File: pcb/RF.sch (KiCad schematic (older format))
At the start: 50 parts, among them P401 CONN_01X02, P402 CONN_01X02, U401 MAX2750, U402 MGA-635P8, U403 HHM1520, U404 MGA-635P8, U405 LT5560, U406 PD2328J, U407 WA04P

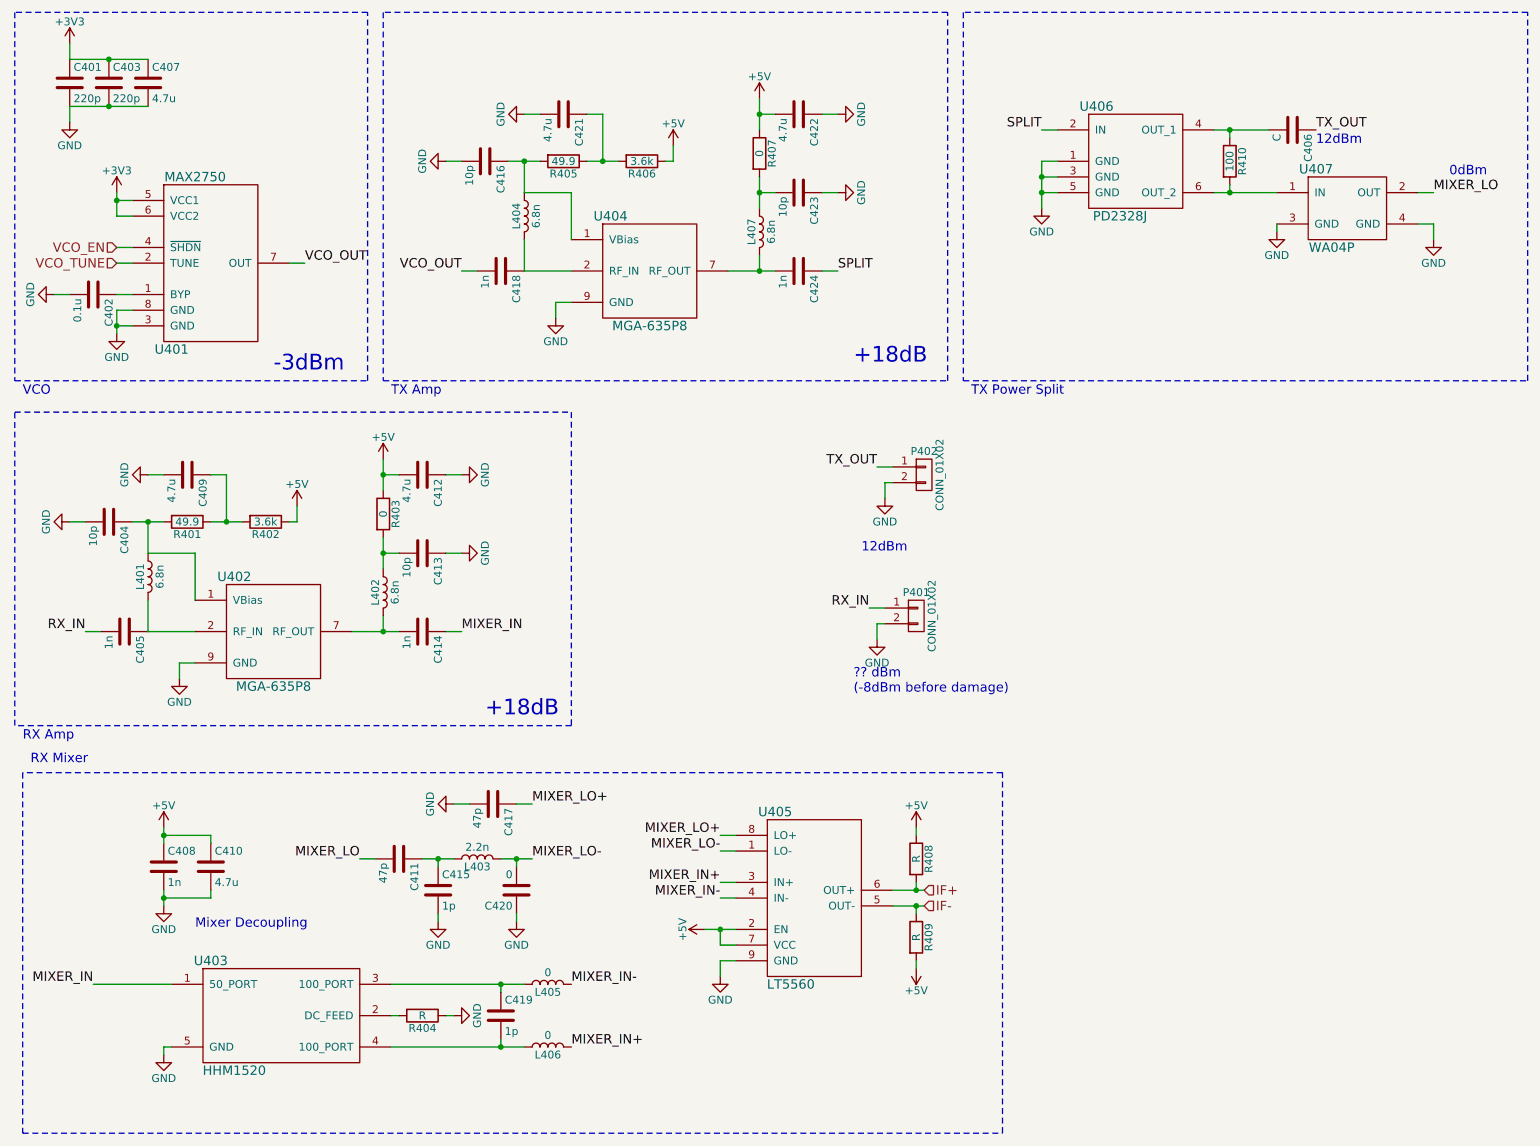
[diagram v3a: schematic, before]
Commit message: First firmware to begin board bringup
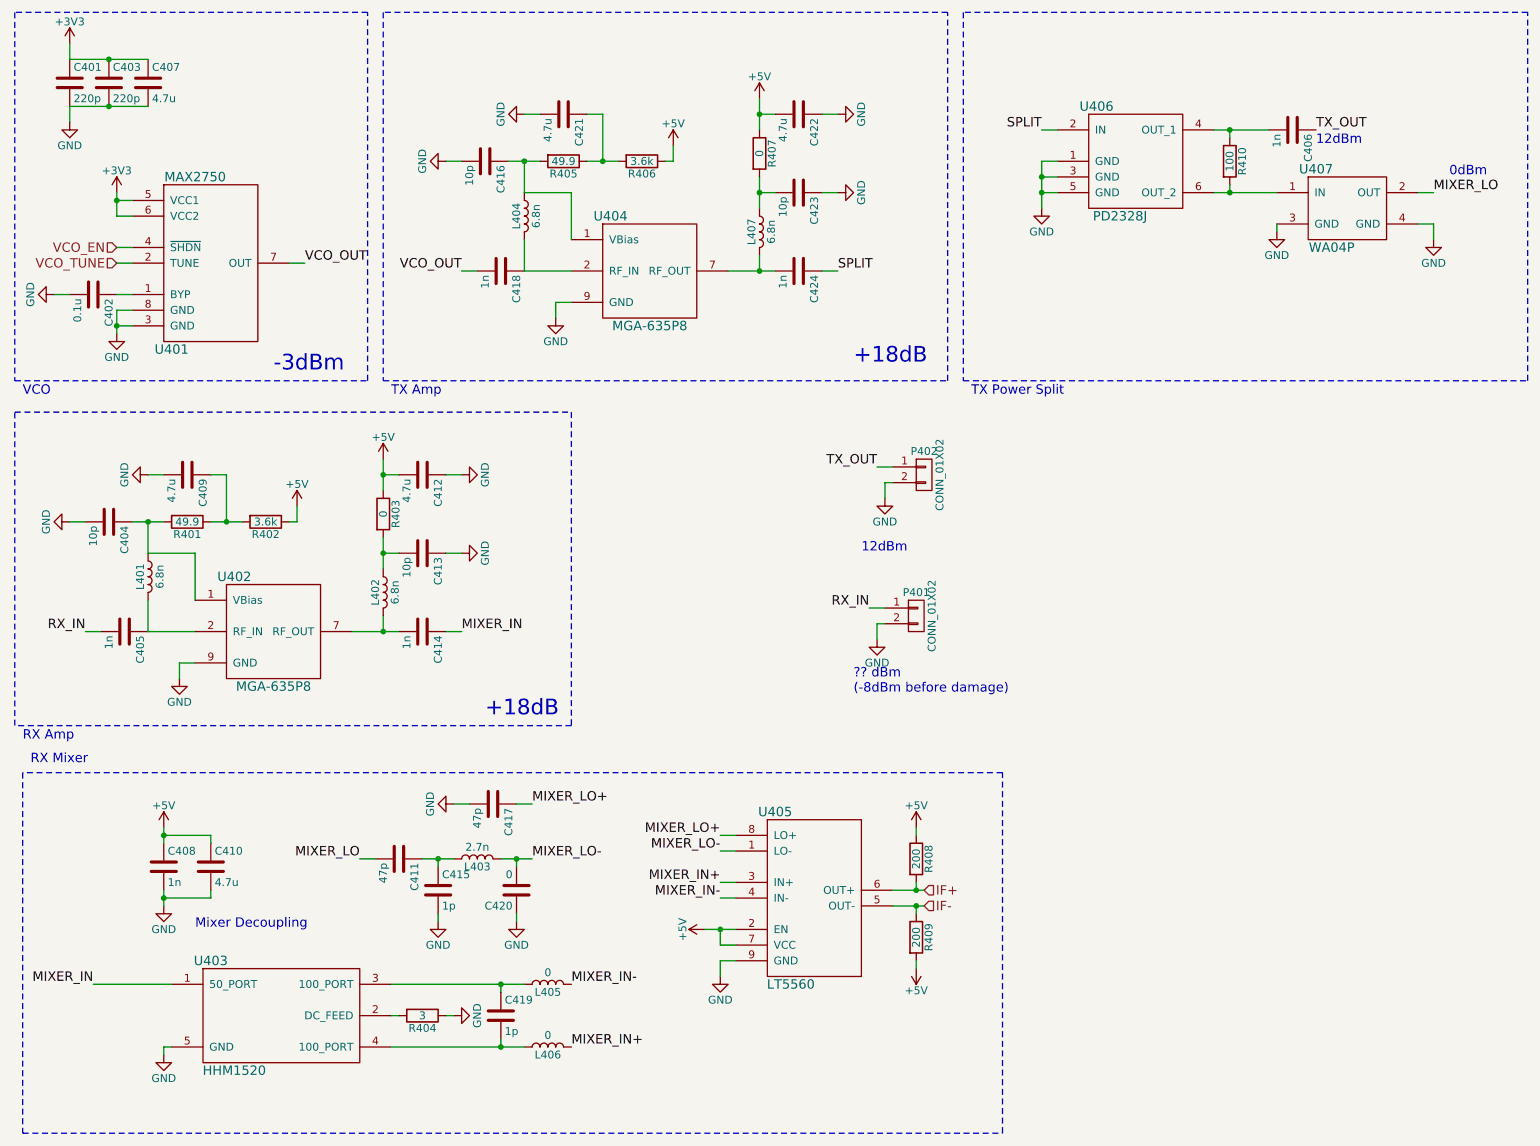
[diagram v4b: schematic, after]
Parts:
- C406: value C -> 1n
- L403: value 2.2n -> 2.7n
- R404: value R -> 3
- R408, R409: value R -> 200
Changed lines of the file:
@@
 $EndComp
 $Comp
-L GND #PWR411
+L GND #PWR043
 U 1 1 58AA10B9
 P 1600 4800
-F 0 "#PWR411" H 1600 4550 50  0001 C CNN
+F 0 "#PWR043" H 1600 4550 50  0001 C CNN
 F 1 "GND" H 1600 4650 50  0000 C CNN
 F 2 "" H 1600 4800 50  0000 C CNN
@@
 $EndComp
 $Comp
-L GND #PWR404
+L GND #PWR044
 U 1 1 58AA10EF
 P 900 3800
-F 0 "#PWR404" H 900 3550 50  0001 C CNN
+F 0 "#PWR044" H 900 3550 50  0001 C CNN
 F 1 "GND" H 900 3650 50  0000 C CNN
 F 2 "" H 900 3800 50  0000 C CNN
@@
 $EndComp
 $Comp
-L GND #PWR407
+L GND #PWR045
 U 1 1 58AA1125
 P 1400 3500
-F 0 "#PWR407" H 1400 3250 50  0001 C CNN
+F 0 "#PWR045" H 1400 3250 50  0001 C CNN
 F 1 "GND" H 1400 3350 50  0000 C CNN
 F 2 "" H 1400 3500 50  0000 C CNN
@@
 $EndComp
 $Comp
-L GND #PWR419
+L GND #PWR046
 U 1 1 58AA115B
 P 3400 4000
-F 0 "#PWR419" H 3400 3750 50  0001 C CNN
+F 0 "#PWR046" H 3400 3750 50  0001 C CNN
 F 1 "GND" H 3400 3850 50  0000 C CNN
 F 2 "" H 3400 4000 50  0000 C CNN
@@
 $EndComp
 $Comp
-L GND #PWR418
+L GND #PWR047
 U 1 1 58AA1191
 P 3400 3500
-F 0 "#PWR418" H 3400 3250 50  0001 C CNN
+F 0 "#PWR047" H 3400 3250 50  0001 C CNN
 F 1 "GND" H 3400 3350 50  0000 C CNN
 F 2 "" H 3400 3500 50  0000 C CNN
@@
 $EndComp
 $Comp
-L +5V #PWR413
+L +5V #PWR048
 U 1 1 58AA11C7
 P 2900 3400
-F 0 "#PWR413" H 2900 3250 50  0001 C CNN
+F 0 "#PWR048" H 2900 3250 50  0001 C CNN
 F 1 "+5V" H 2900 3540 50  0000 C CNN
 F 2 "" H 2900 3400 50  0000 C CNN
@@
 $EndComp
 $Comp
-L +5V #PWR412
+L +5V #PWR049
 U 1 1 58AA11FD
 P 2350 3700
-F 0 "#PWR412" H 2350 3550 50  0001 C CNN
+F 0 "#PWR049" H 2350 3550 50  0001 C CNN
 F 1 "+5V" H 2350 3840 50  0000 C CNN
 F 2 "" H 2350 3700 50  0000 C CNN
@@
 P 3150 6950
 F 0 "R404" V 3230 6950 50  0000 C CNN
-F 1 "R" V 3150 6950 50  0000 C CNN
+F 1 "3" V 3150 6950 50  0000 C CNN
 F 2 "Resistors_SMD:R_0402" V 3080 6950 50  0001 C CNN
 F 3 "" H 3150 6950 50  0000 C CNN
@@
 $EndComp
 $Comp
-L GND #PWR417
+L GND #PWR050
 U 1 1 58AA2399
 P 3350 6950
-F 0 "#PWR417" H 3350 6700 50  0001 C CNN
+F 0 "#PWR050" H 3350 6700 50  0001 C CNN
 F 1 "GND" H 3350 6800 50  0000 C CNN
 F 2 "" H 3350 6950 50  0000 C CNN
@@
 P 3500 5950
 F 0 "L403" V 3450 5950 50  0000 C CNN
-F 1 "2.2n" V 3575 5950 50  0000 C CNN
+F 1 "2.7n" V 3575 5950 50  0000 C CNN
 F 2 "Capacitors_SMD:C_0402" H 3500 5950 50  0001 C CNN
 F 3 "" H 3500 5950 50  0000 C CNN
@@
 $EndComp
 $Comp
-L GND #PWR420
+L GND #PWR051
 U 1 1 58AA2A6C
 P 3750 6350
-F 0 "#PWR420" H 3750 6100 50  0001 C CNN
+F 0 "#PWR051" H 3750 6100 50  0001 C CNN
 F 1 "GND" H 3750 6200 50  0000 C CNN
 F 2 "" H 3750 6350 50  0000 C CNN
@@
 $EndComp
 $Comp
-L GND #PWR414
+L GND #PWR052
 U 1 1 58AA2AB8
 P 3250 6350
-F 0 "#PWR414" H 3250 6100 50  0001 C CNN
+F 0 "#PWR052" H 3250 6100 50  0001 C CNN
 F 1 "GND" H 3250 6200 50  0000 C CNN
 F 2 "" H 3250 6350 50  0000 C CNN
@@
 $EndComp
 $Comp
-L GND #PWR410
+L GND #PWR053
 U 1 1 58AA2B04
 P 1500 7200
-F 0 "#PWR410" H 1500 6950 50  0001 C CNN
+F 0 "#PWR053" H 1500 6950 50  0001 C CNN
 F 1 "GND" H 1500 7050 50  0000 C CNN
 F 2 "" H 1500 7200 50  0000 C CNN
@@
 $EndComp
 $Comp
-L GND #PWR416
+L GND #PWR054
 U 1 1 58AA32CA
 P 3350 5600
-F 0 "#PWR416" H 3350 5350 50  0001 C CNN
+F 0 "#PWR054" H 3350 5350 50  0001 C CNN
 F 1 "GND" H 3350 5450 50  0000 C CNN
 F 2 "" H 3350 5600 50  0000 C CNN
@@
 MIXER_IN+
 $Comp
-L GND #PWR425
+L GND #PWR055
 U 1 1 58AA3ACB
 P 5050 6700
-F 0 "#PWR425" H 5050 6450 50  0001 C CNN
+F 0 "#PWR055" H 5050 6450 50  0001 C CNN
 F 1 "GND" H 5050 6550 50  0000 C CNN
 F 2 "" H 5050 6700 50  0000 C CNN
@@
 $EndComp
 $Comp
-L GND #PWR409
+L GND #PWR056
 U 1 1 58AA3E57
 P 1500 6250
-F 0 "#PWR409" H 1500 6000 50  0001 C CNN
+F 0 "#PWR056" H 1500 6000 50  0001 C CNN
 F 1 "GND" H 1500 6100 50  0000 C CNN
 F 2 "" H 1500 6250 50  0000 C CNN
@@
 $EndComp
 $Comp
-L +5V #PWR408
+L +5V #PWR057
 U 1 1 58AA4282
 P 1500 5750
-F 0 "#PWR408" H 1500 5600 50  0001 C CNN
+F 0 "#PWR057" H 1500 5600 50  0001 C CNN
 F 1 "+5V" H 1500 5890 50  0000 C CNN
 F 2 "" H 1500 5750 50  0000 C CNN
@@
 $EndComp
 $Comp
-L +5V #PWR424
+L +5V #PWR058
 U 1 1 58AA42F1
 P 4950 6400
-F 0 "#PWR424" H 4950 6250 50  0001 C CNN
+F 0 "#PWR058" H 4950 6250 50  0001 C CNN
 F 1 "+5V" H 4950 6540 50  0000 C CNN
 F 2 "" H 4950 6400 50  0000 C CNN
@@
 P 6300 6450
 F 0 "R409" V 6380 6450 50  0000 C CNN
-F 1 "R" V 6300 6450 50  0000 C CNN
+F 1 "200" V 6300 6450 50  0000 C CNN
 F 2 "Resistors_SMD:R_0402" V 6230 6450 50  0001 C CNN
 F 3 "" H 6300 6450 50  0000 C CNN
@@
 P 6300 5950
 F 0 "R408" V 6380 5950 50  0000 C CNN
-F 1 "R" V 6300 5950 50  0000 C CNN
+F 1 "200" V 6300 5950 50  0000 C CNN
 F 2 "Resistors_SMD:R_0402" V 6230 5950 50  0001 C CNN
 F 3 "" H 6300 5950 50  0000 C CNN
@@
 $EndComp
 $Comp
-L +5V #PWR432
+L +5V #PWR059
 U 1 1 58AA4D6B
 P 6300 6650
-F 0 "#PWR432" H 6300 6500 50  0001 C CNN
+F 0 "#PWR059" H 6300 6500 50  0001 C CNN
 F 1 "+5V" H 6300 6790 50  0000 C CNN
 F 2 "" H 6300 6650 50  0000 C CNN
@@
 $EndComp
 $Comp
-L +5V #PWR431
+L +5V #PWR060
 U 1 1 58AA4DBF
 P 6300 5750
-F 0 "#PWR431" H 6300 5600 50  0001 C CNN
+F 0 "#PWR060" H 6300 5600 50  0001 C CNN
 F 1 "+5V" H 6300 5890 50  0000 C CNN
 F 2 "" H 6300 5750 50  0000 C CNN
@@
 $EndComp
 $Comp
-L GND #PWR422
+L GND #PWR061
 U 1 1 58AA62C7
 P 4000 2500
-F 0 "#PWR422" H 4000 2250 50  0001 C CNN
+F 0 "#PWR061" H 4000 2250 50  0001 C CNN
 F 1 "GND" H 4000 2350 50  0000 C CNN
 F 2 "" H 4000 2500 50  0000 C CNN
@@
 $EndComp
 $Comp
-L GND #PWR415
+L GND #PWR062
 U 1 1 58AA62CD
 P 3300 1500
-F 0 "#PWR415" H 3300 1250 50  0001 C CNN
+F 0 "#PWR062" H 3300 1250 50  0001 C CNN
 F 1 "GND" H 3300 1350 50  0000 C CNN
 F 2 "" H 3300 1500 50  0000 C CNN
@@
 $EndComp
 $Comp
-L GND #PWR421
+L GND #PWR063
 U 1 1 58AA62D3
 P 3800 1200
-F 0 "#PWR421" H 3800 950 50  0001 C CNN
+F 0 "#PWR063" H 3800 950 50  0001 C CNN
 F 1 "GND" H 3800 1050 50  0000 C CNN
 F 2 "" H 3800 1200 50  0000 C CNN
@@
 $EndComp
 $Comp
-L GND #PWR428
+L GND #PWR064
 U 1 1 58AA62D9
 P 5800 1700
-F 0 "#PWR428" H 5800 1450 50  0001 C CNN
+F 0 "#PWR064" H 5800 1450 50  0001 C CNN
 F 1 "GND" H 5800 1550 50  0000 C CNN
 F 2 "" H 5800 1700 50  0000 C CNN
@@
 $EndComp
 $Comp
-L GND #PWR427
+L GND #PWR065
 U 1 1 58AA62DF
 P 5800 1200
-F 0 "#PWR427" H 5800 950 50  0001 C CNN
+F 0 "#PWR065" H 5800 950 50  0001 C CNN
 F 1 "GND" H 5800 1050 50  0000 C CNN
 F 2 "" H 5800 1200 50  0000 C CNN
@@
 $EndComp
 $Comp
-L +5V #PWR426
+L +5V #PWR066
 U 1 1 58AA62E5
 P 5300 1100
-F 0 "#PWR426" H 5300 950 50  0001 C CNN
+F 0 "#PWR066" H 5300 950 50  0001 C CNN
 F 1 "+5V" H 5300 1240 50  0000 C CNN
 F 2 "" H 5300 1100 50  0000 C CNN
@@
 $EndComp
 $Comp
-L +5V #PWR423
+L +5V #PWR067
 U 1 1 58AA62EB
 P 4750 1400
-F 0 "#PWR423" H 4750 1250 50  0001 C CNN
+F 0 "#PWR067" H 4750 1250 50  0001 C CNN
 F 1 "+5V" H 4750 1540 50  0000 C CNN
 F 2 "" H 4750 1400 50  0000 C CNN
@@
 $EndComp
 $Comp
-L +3V3 #PWR402
+L +3V3 #PWR068
 U 1 1 58AA6803
 P 900 750
-F 0 "#PWR402" H 900 600 50  0001 C CNN
+F 0 "#PWR068" H 900 600 50  0001 C CNN
 F 1 "+3V3" H 900 890 50  0000 C CNN
 F 2 "" H 900 750 50  0000 C CNN
@@
 $EndComp
 $Comp
-L +3V3 #PWR405
+L +3V3 #PWR069
 U 1 1 58AA6877
 P 1200 1700
-F 0 "#PWR405" H 1200 1550 50  0001 C CNN
+F 0 "#PWR069" H 1200 1550 50  0001 C CNN
 F 1 "+3V3" H 1200 1840 50  0000 C CNN
 F 2 "" H 1200 1700 50  0000 C CNN
@@
 $EndComp
 $Comp
-L GND #PWR403
+L GND #PWR070
 U 1 1 58AA68EB
 P 900 1250
-F 0 "#PWR403" H 900 1000 50  0001 C CNN
+F 0 "#PWR070" H 900 1000 50  0001 C CNN
 F 1 "GND" H 900 1100 50  0000 C CNN
 F 2 "" H 900 1250 50  0000 C CNN
@@
 $EndComp
 $Comp
-L GND #PWR406
+L GND #PWR071
 U 1 1 58AA695F
 P 1200 2600
-F 0 "#PWR406" H 1200 2350 50  0001 C CNN
+F 0 "#PWR071" H 1200 2350 50  0001 C CNN
 F 1 "GND" H 1200 2450 50  0000 C CNN
 F 2 "" H 1200 2600 50  0000 C CNN
@@
 $EndComp
 $Comp
-L GND #PWR401
+L GND #PWR072
 U 1 1 58AA69D3
 P 800 2350
-F 0 "#PWR401" H 800 2100 50  0001 C CNN
+F 0 "#PWR072" H 800 2100 50  0001 C CNN
 F 1 "GND" H 800 2200 50  0000 C CNN
 F 2 "" H 800 2350 50  0000 C CNN
@@
 VCO_OUT
 $Comp
-L GND #PWR433
+L GND #PWR073
 U 1 1 58AA8C7D
 P 7100 1800
-F 0 "#PWR433" H 7100 1550 50  0001 C CNN
+F 0 "#PWR073" H 7100 1550 50  0001 C CNN
 F 1 "GND" H 7100 1650 50  0000 C CNN
 F 2 "" H 7100 1800 50  0000 C CNN
@@
 $EndComp
 $Comp
-L GND #PWR434
+L GND #PWR074
 U 1 1 58AA97AD
 P 8600 1950
-F 0 "#PWR434" H 8600 1700 50  0001 C CNN
+F 0 "#PWR074" H 8600 1700 50  0001 C CNN
 F 1 "GND" H 8600 1800 50  0000 C CNN
 F 2 "" H 8600 1950 50  0000 C CNN
@@
 $EndComp
 $Comp
-L GND #PWR435
+L GND #PWR075
 U 1 1 58AA9851
 P 9600 2000
-F 0 "#PWR435" H 9600 1750 50  0001 C CNN
+F 0 "#PWR075" H 9600 1750 50  0001 C CNN
 F 1 "GND" H 9600 1850 50  0000 C CNN
 F 2 "" H 9600 2000 50  0000 C CNN
@@
 $EndComp
 $Comp
-L GND #PWR430
+L GND #PWR076
 U 1 1 58AAC543
 P 6100 3650
-F 0 "#PWR430" H 6100 3400 50  0001 C CNN
+F 0 "#PWR076" H 6100 3400 50  0001 C CNN
 F 1 "GND" H 6100 3500 50  0000 C CNN
 F 2 "" H 6100 3650 50  0000 C CNN
@@
 $EndComp
 $Comp
-L GND #PWR429
+L GND #PWR077
 U 1 1 58AAC5BB
 P 6050 4550
-F 0 "#PWR429" H 6050 4300 50  0001 C CNN
+F 0 "#PWR077" H 6050 4300 50  0001 C CNN
 F 1 "GND" H 6050 4400 50  0000 C CNN
 F 2 "" H 6050 4550 50  0000 C CNN
@@
 P 8700 1300
 F 0 "C406" H 8725 1400 50  0000 L CNN
-F 1 "C" H 8725 1200 50  0000 L CNN
+F 1 "1n" H 8725 1200 50  0000 L CNN
 F 2 "Capacitors_SMD:C_0402" H 8738 1150 50  0001 C CNN
 F 3 "" H 8700 1300 50  0000 C CNN

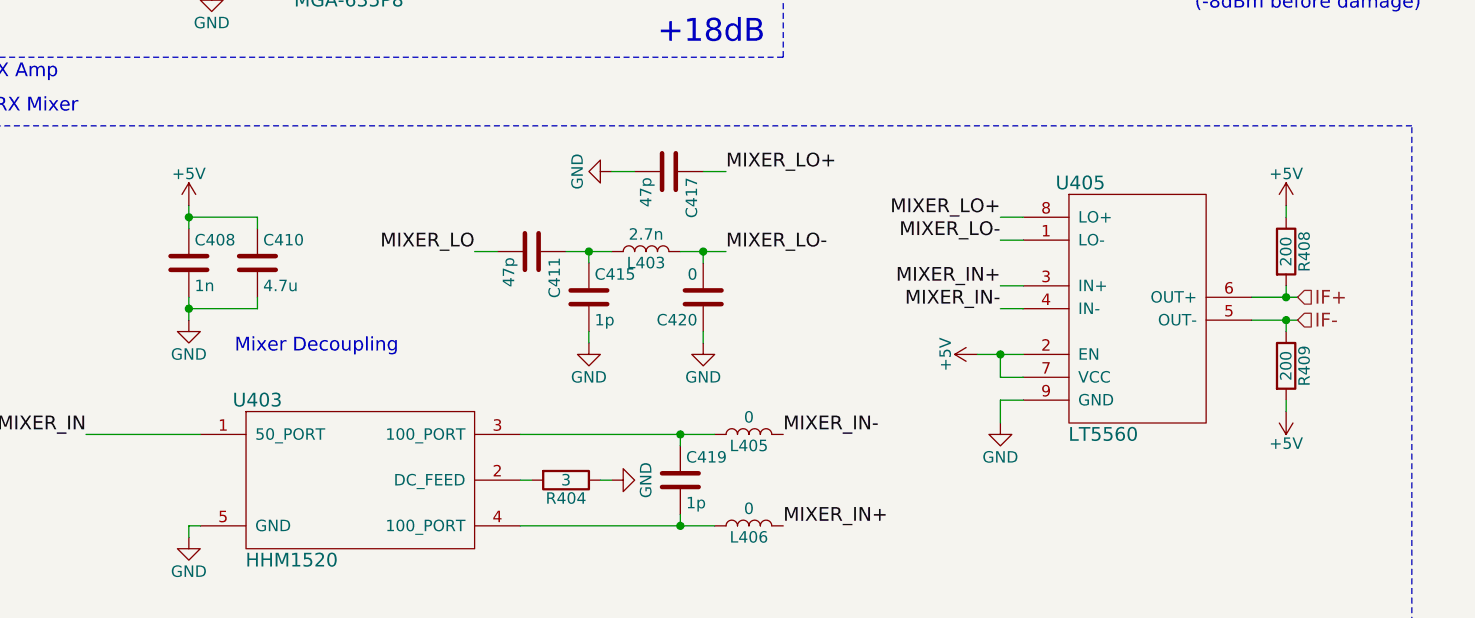
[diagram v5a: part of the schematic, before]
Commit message: added PA board
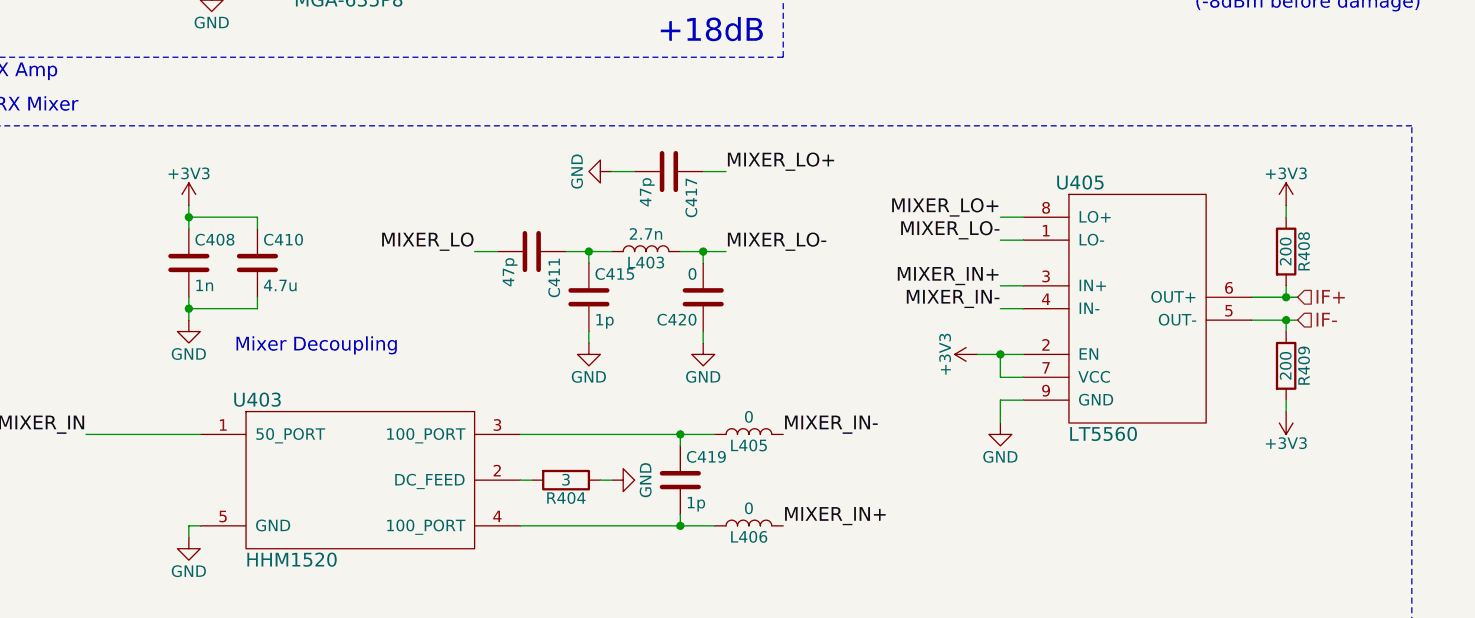
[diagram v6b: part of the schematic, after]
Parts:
- P401, P402: footprint wbraun_smd:SMA-Edge-short -> wbraun_smd:SMA-Edge-China-Short
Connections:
- net +3V3: now also C408.1, C410.1, R408.1, R409.2, U405.2 (EN), U405.7 (VCC)
- net +5V: no longer C408.1, C410.1, R408.1, R409.2, U405.2 (EN), U405.7 (VCC)
